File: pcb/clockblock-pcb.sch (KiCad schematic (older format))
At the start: 62 parts

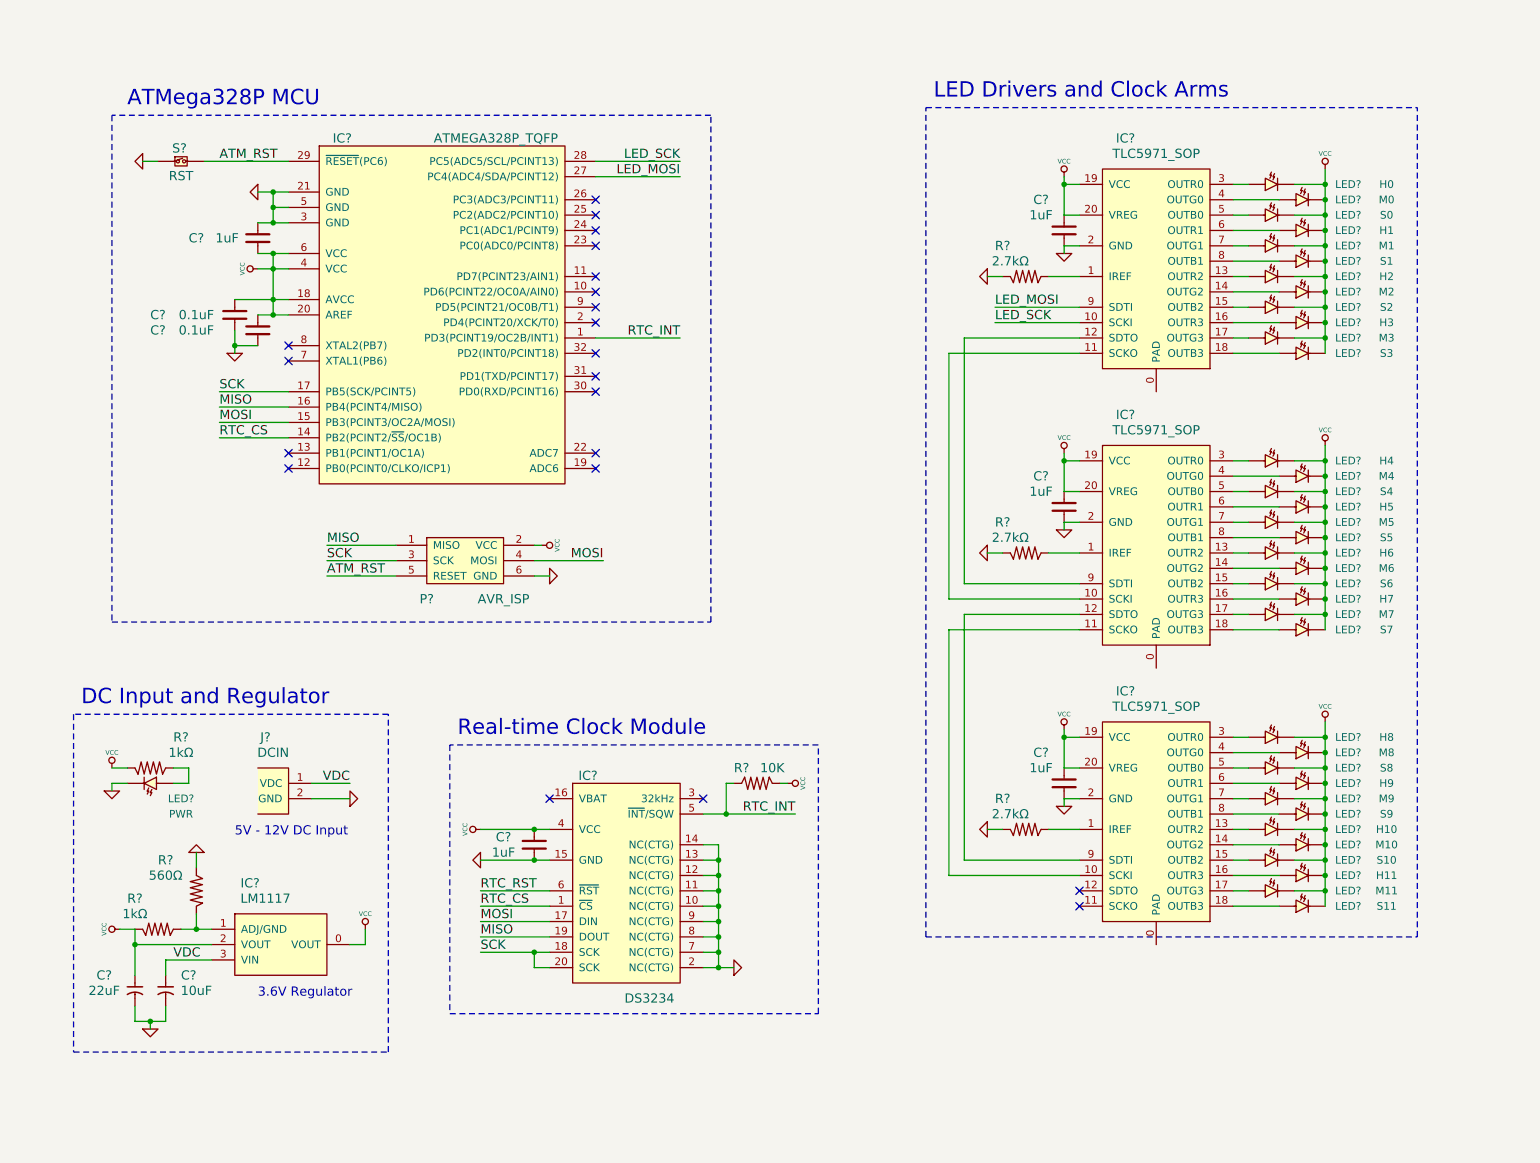
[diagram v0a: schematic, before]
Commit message: fixed incorrect LED polarity, added arm headers, and added a backup coincell for the RTC
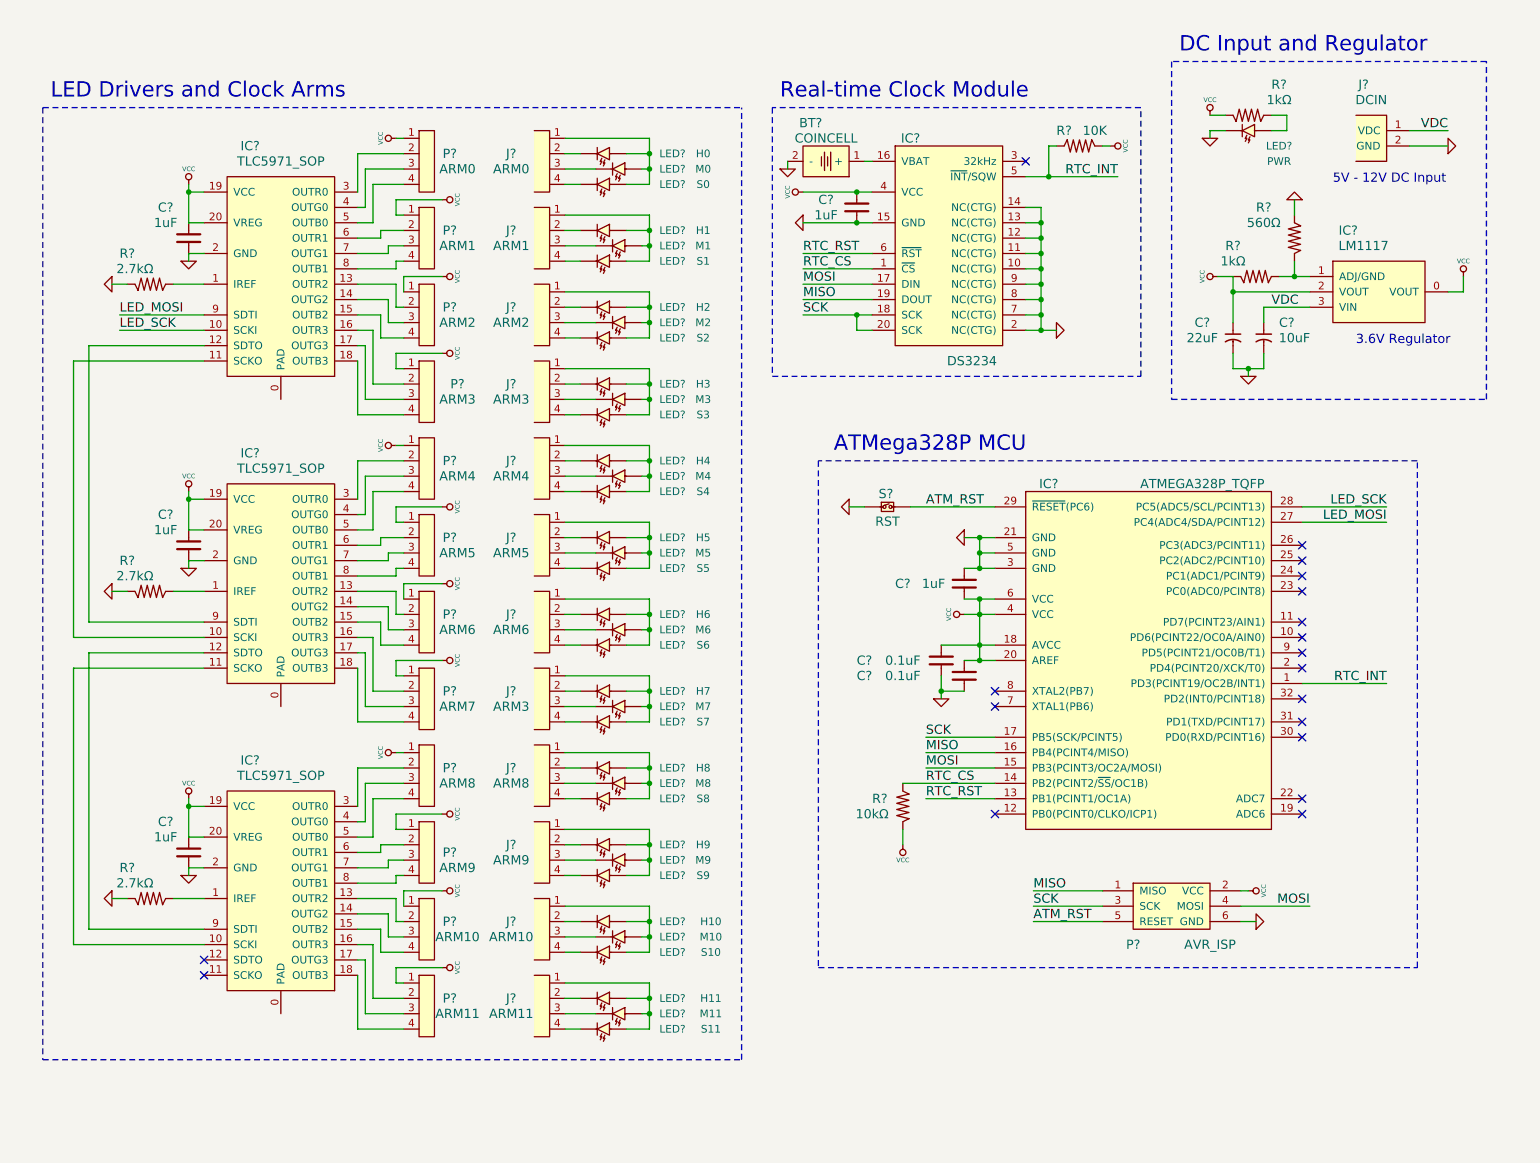
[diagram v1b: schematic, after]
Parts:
- removed LED?: H8, ~, symbol LED
- removed LED?: M8, ~, symbol LED
- removed LED?: S8, ~, symbol LED
- removed LED?: H9, ~, symbol LED
- removed LED?: M9, ~, symbol LED
- removed LED?: S9, ~, symbol LED
- removed LED?: H10, ~, symbol LED
- removed LED?: M10, ~, symbol LED
- removed LED?: S10, ~, symbol LED
- removed LED?: H11, ~, symbol LED
- removed LED?: M11, ~, symbol LED
- removed LED?: S11, ~, symbol LED
- removed LED?: H4, ~, symbol LED
- removed LED?: M4, ~, symbol LED
- removed LED?: S4, ~, symbol LED
- removed LED?: H5, ~, symbol LED
- removed LED?: M5, ~, symbol LED
- removed LED?: S5, ~, symbol LED
- removed LED?: H6, ~, symbol LED
- removed LED?: M6, ~, symbol LED
- removed LED?: S6, ~, symbol LED
- removed LED?: H7, ~, symbol LED
- removed LED?: M7, ~, symbol LED
- removed LED?: S7, ~, symbol LED
- removed LED?: H1, ~, symbol LED
- removed LED?: M1, ~, symbol LED
- removed LED?: S1, ~, symbol LED
- removed LED?: H2, ~, symbol LED
- removed LED?: M2, ~, symbol LED
- removed LED?: S2, ~, symbol LED
- removed LED?: H3, ~, symbol LED
- removed LED?: M3, ~, symbol LED
- removed LED?: S3, ~, symbol LED
- added BT?: COINCELL, symbol BATTERY
- added J?: ARM0, ~, symbol 4PIN_FEMALE
- added J?: ARM1, ~, symbol 4PIN_FEMALE
- added J?: ARM2, ~, symbol 4PIN_FEMALE
- added J? (x2): ARM3, ~, symbol 4PIN_FEMALE
- added J?: ARM4, ~, symbol 4PIN_FEMALE
- added J?: ARM5, ~, symbol 4PIN_FEMALE
- added J?: ARM6, ~, symbol 4PIN_FEMALE
- added J?: ARM8, ~, symbol 4PIN_FEMALE
- added J?: ARM9, ~, symbol 4PIN_FEMALE
- added J?: ARM10, ~, symbol 4PIN_FEMALE
- added J?: ARM11, ~, symbol 4PIN_FEMALE
- added LED?: H1, ~, symbol LED
- added LED?: M1, ~, symbol LED
- added LED?: S1, ~, symbol LED
- added LED?: H2, ~, symbol LED
- added LED?: M2, ~, symbol LED
- added LED?: S2, ~, symbol LED
- added LED?: H3, ~, symbol LED
- added LED?: M3, ~, symbol LED
- added LED?: S3, ~, symbol LED
- added LED?: H4, ~, symbol LED
- added LED?: M4, ~, symbol LED
- added LED?: S4, ~, symbol LED
- added LED?: H5, ~, symbol LED
- added LED?: M5, ~, symbol LED
- added LED?: S5, ~, symbol LED
- added LED?: H6, ~, symbol LED
- added LED?: M6, ~, symbol LED
- added LED?: S6, ~, symbol LED
- added LED?: H7, ~, symbol LED
- added LED?: M7, ~, symbol LED
- added LED?: S7, ~, symbol LED
- added LED?: H8, ~, symbol LED
- added LED?: M8, ~, symbol LED
- added LED?: S8, ~, symbol LED
- added LED?: H9, ~, symbol LED
- added LED?: M9, ~, symbol LED
- added LED?: S9, ~, symbol LED
- added LED?: H10, ~, symbol LED
- added LED?: M10, ~, symbol LED
- added LED?: S10, ~, symbol LED
- added LED?: H11, ~, symbol LED
- added LED?: M11, ~, symbol LED
- added LED?: S11, ~, symbol LED
- added P?: ARM0, ~, symbol 4PIN_HEADER
- added P?: ARM1, ~, symbol 4PIN_HEADER
- added P?: ARM2, ~, symbol 4PIN_HEADER
- added P?: ARM3, ~, symbol 4PIN_HEADER
- added P?: ARM4, ~, symbol 4PIN_HEADER
- added P?: ARM5, ~, symbol 4PIN_HEADER
- added P?: ARM6, ~, symbol 4PIN_HEADER
- added P?: ARM7, ~, symbol 4PIN_HEADER
- added P?: ARM8, ~, symbol 4PIN_HEADER
- added P?: ARM9, ~, symbol 4PIN_HEADER
- added P?: ARM10, ~, symbol 4PIN_HEADER
- added P?: ARM11, ~, symbol 4PIN_HEADER
- added R?: 10kΩ, ~, symbol R
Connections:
- net GND: now also BT?.2 (-)
- net RTC_CS: now also R?.2
- net RTC_RST: now also IC?.13 (PB1(PCINT1/OC1A))
- net VCC: now also P?.1, P?.1, P?.1, P?.1, P?.1, P?.1, P?.1, P?.1, P?.1, P?.1, P?.1, P?.1, R?.1; no longer LED?.1 (C), LED?.1 (C), LED?.1 (C)
- net at IC?.16 (VBAT): now also BT?.1 (+)
- net at IC?.13 (OUTR2): now also P?.2 (x3)
- net at IC?.14 (OUTG2): now also P?.3 (x3)
- net at IC?.15 (OUTB2): now also P?.4 (x3)
- net at IC?.16 (OUTR3): now also P?.2 (x3)
- net at IC?.17 (OUTG3): now also P?.3 (x3)
- net at IC?.18 (OUTB3): now also P?.4 (x3)
- net at IC?.3 (OUTR0): now also P?.2 (x2)
- net at IC?.4 (OUTG0): now also P?.3 (x2)
- net at IC?.5 (OUTB0): now also P?.4 (x2)
- net at IC?.6 (OUTR1): now also P?.2 (x3)
- net at IC?.7 (OUTG1): now also P?.3 (x3)
- net at IC?.8 (OUTB1): now also P?.4 (x3)
- net at IC?.3 (OUTR0): now also P?.2; no longer LED?.2 (A)
- net at IC?.4 (OUTG0): now also P?.3; no longer LED?.2 (A)
- net at IC?.5 (OUTB0): now also P?.4; no longer LED?.2 (A)
- new net: J?.2, LED?.1 (C) (x12)
- new net: J?.1, LED?.2 (A), LED?.2 (A), LED?.2 (A) (x12)
- new net: J?.3, LED?.1 (C) (x12)
- new net: J?.4, LED?.1 (C) (x12)
- no-connect marks 21 -> 19
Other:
- moved on the sheet: C?, IC?, J?, LED?, P?, R?, S?

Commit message: annotated schematic and fixed up a component pin type error
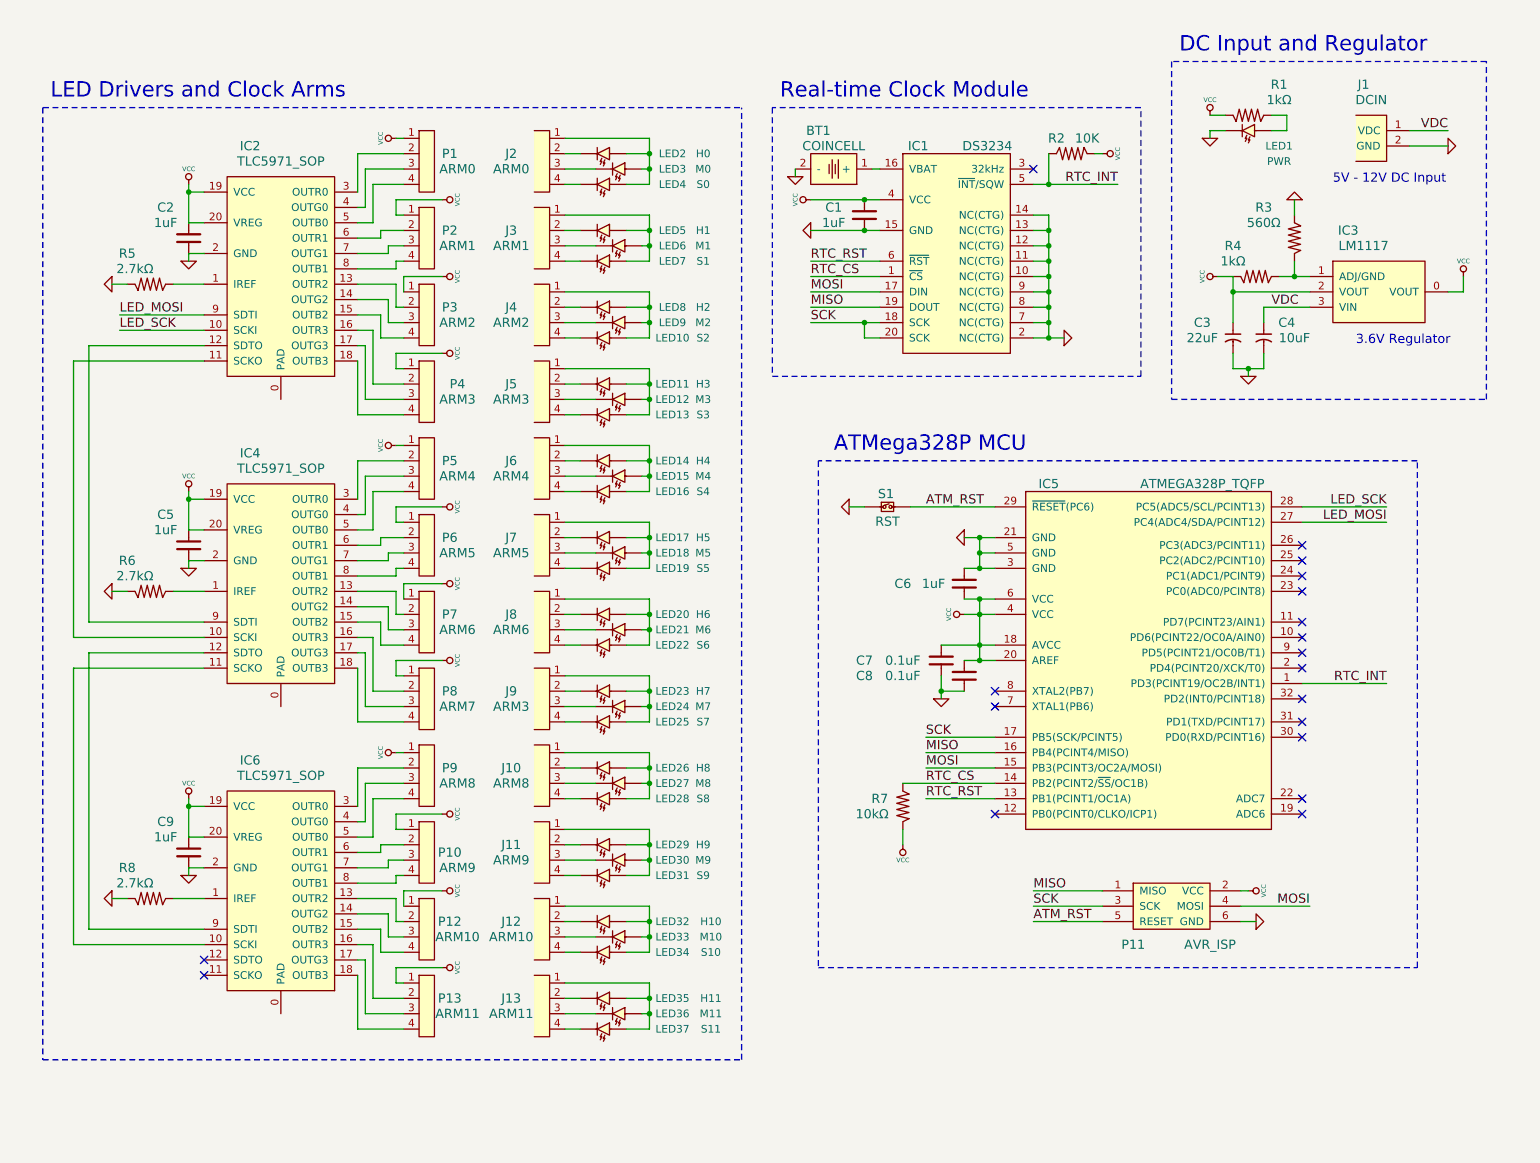
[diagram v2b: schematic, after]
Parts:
- gave numbers to parts that had none: 88
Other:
- moved on the sheet: BT1, C1, IC1, R2

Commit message: component footprints done, moving onto layout
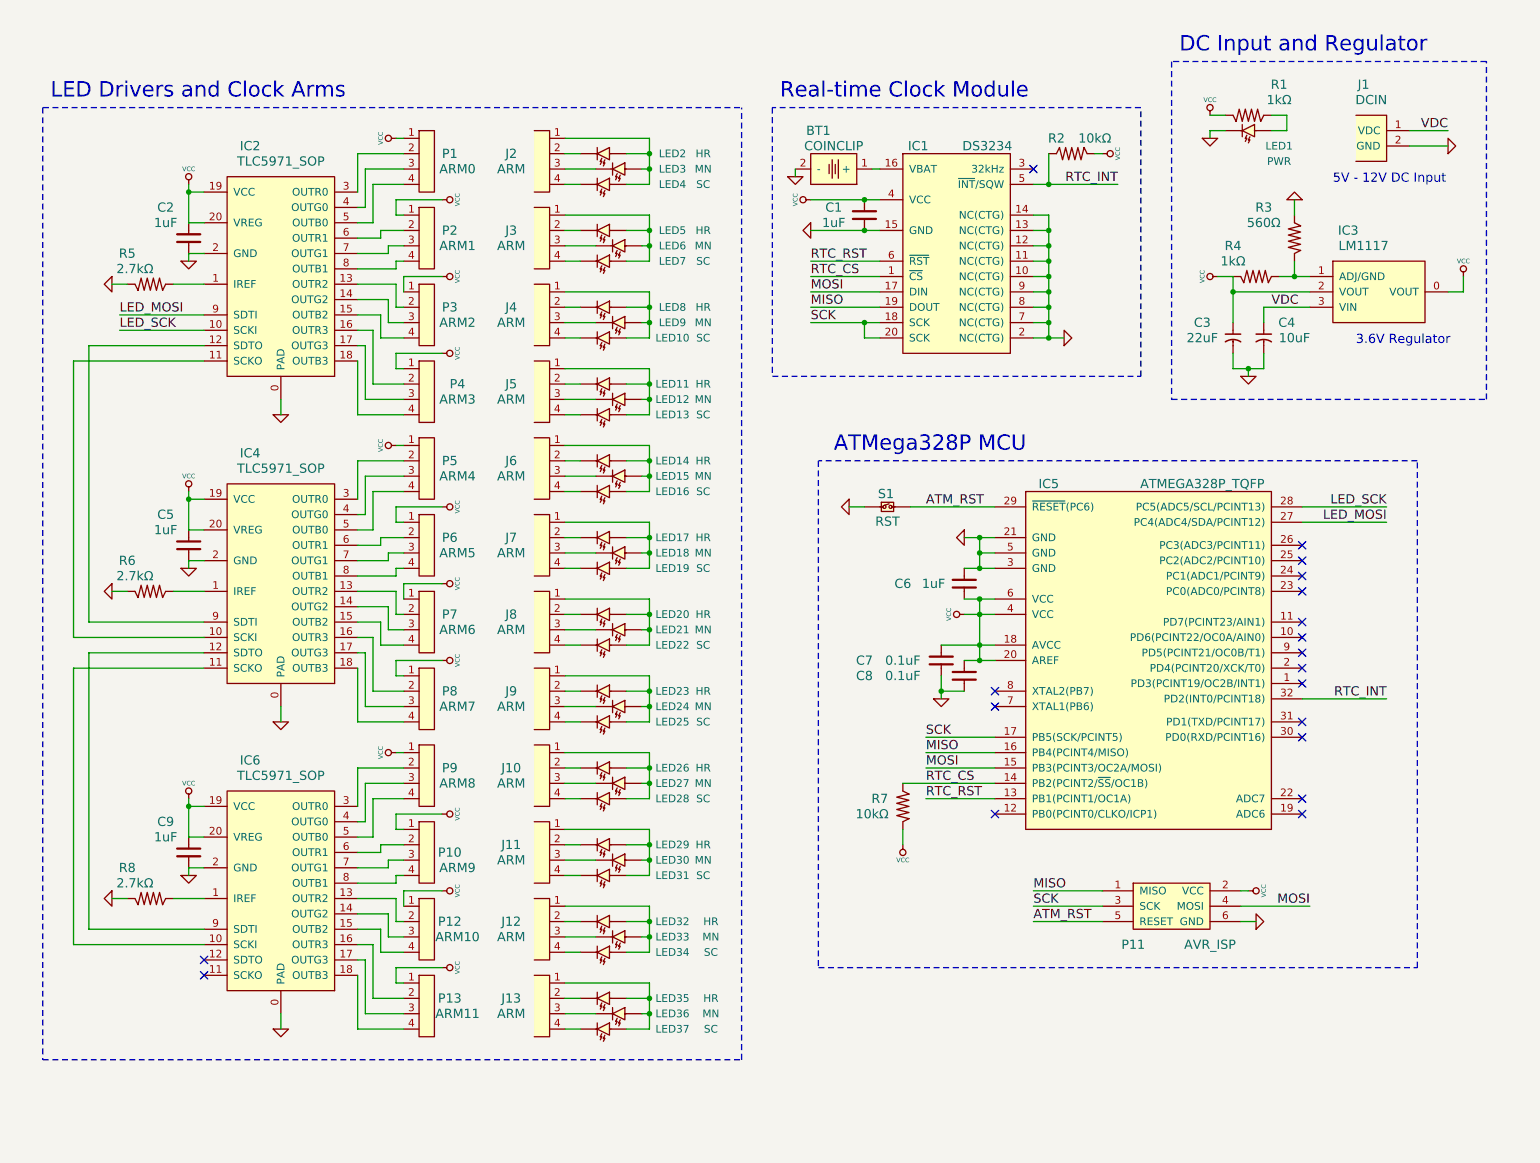
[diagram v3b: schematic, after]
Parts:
- BT1: value COINCELL -> COINCLIP
- J10: value ARM8 -> ARM
- J11: value ARM9 -> ARM
- J12: value ARM10 -> ARM
- J13: value ARM11 -> ARM
- J2: value ARM0 -> ARM
- J3: value ARM1 -> ARM
- J4: value ARM2 -> ARM
- J5, J9: value ARM3 -> ARM
- J6: value ARM4 -> ARM
- J7: value ARM5 -> ARM
- J8: value ARM6 -> ARM
- LED10: value S2 -> SC
- LED11: value H3 -> HR
- LED12: value M3 -> MN
- LED13: value S3 -> SC
- LED14: value H4 -> HR
- LED15: value M4 -> MN
- LED16: value S4 -> SC
- LED17: value H5 -> HR
- LED18: value M5 -> MN
- LED19: value S5 -> SC
- LED2: value H0 -> HR
- LED20: value H6 -> HR
- LED21: value M6 -> MN
- LED22: value S6 -> SC
- LED23: value H7 -> HR
- LED24: value M7 -> MN
- LED25: value S7 -> SC
- LED26: value H8 -> HR
- LED27: value M8 -> MN
- LED28: value S8 -> SC
- LED29: value H9 -> HR
- LED3: value M0 -> MN
- LED30: value M9 -> MN
- LED31: value S9 -> SC
- LED32: value H10 -> HR
- LED33: value M10 -> MN
- LED34: value S10 -> SC
- LED35: value H11 -> HR
- LED36: value M11 -> MN
- LED37: value S11 -> SC
- LED4: value S0 -> SC
- LED5: value H1 -> HR
- LED6: value M1 -> MN
- LED7: value S1 -> SC
- LED8: value H2 -> HR
- LED9: value M2 -> MN
- R2: value 10K -> 10kΩ
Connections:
- net GND: now also IC2.0 (PAD), IC4.0 (PAD), IC6.0 (PAD)
- net RTC_INT: now also IC5.32 (PD2(INT0/PCINT18)); no longer IC5.1 (PD3(PCINT19/OC2B/INT1))

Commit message: board layout done. double checking then sending to fab
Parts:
- added P14: SERIAL, ~, symbol 4PIN_HEADER
- added R10, R9: 10kΩ, ~, symbol R
- added S2, S3: SET, ~, symbol SPST
- C7: value 0.1uF -> 1uF
- IC2, IC4, IC6: value TLC5971_SOP -> TLC5971
- IC5: value ATMEGA328P_TQFP -> ATMEGA328P
- R3: value 560Ω -> 1kΩ
- R4: value 1kΩ -> 560Ω
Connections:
- net GND: now also C7.2, C8.2, P14.4, S2.2, S3.2; no longer C7.1, C8.1
- net RTC_CS: now also IC5.25 (PC2(ADC2/PCINT10)); no longer IC5.14 (PB2(PCINT2/~SS~/OC1B))
- net RTC_RST: now also IC5.26 (PC3(ADC3/PCINT11)); no longer IC5.13 (PB1(PCINT1/OC1A))
- net VCC: now also C7.1, C8.1, P14.3, R10.2, R9.2; no longer C7.2, C8.2
- net at IC5.10 (PD6(PCINT22/OC0A/AIN0)): now also R10.1, S3.1
- net at IC5.11 (PD7(PCINT23/AIN1)): now also R9.1, S2.1
- net at IC5.30 (PD0(RXD/PCINT16)): now also P14.2
- net at IC5.31 (PD1(TXD/PCINT17)): now also P14.1
- no-connect marks 19 -> 15
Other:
- note added: "3.5V Regulator"
- note removed: "3.6V Regulator"
- moved on the sheet: C6, C7, C8, R7

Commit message: moving on to v0.2 schematic
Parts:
- removed BT1: COINCLIP, symbol BATTERY
- removed C1: 1uF, ~, symbol C
- removed IC1: DS3234, symbol DS3234
- removed J1: DCIN, symbol DCIN
- removed J10, J11, J12, J13, J2, J3, J4, J5, J6, J7, J8, J9: ARM, ~, symbol 4PIN_FEMALE
- removed LED10, LED13, LED16, LED19, LED22, LED25, LED28, LED31, LED34, LED37, LED4, LED7: SC, ~, symbol LED
- removed LED11, LED14, LED17, LED2, LED20, LED23, LED26, LED29, LED32, LED35, LED5, LED8: HR, ~, symbol LED
- removed LED12, LED15, LED18, LED21, LED24, LED27, LED3, LED30, LED33, LED36, LED6, LED9: MN, ~, symbol LED
- removed P14: SERIAL, ~, symbol 4PIN_HEADER
- removed R2, R7: 10kΩ, ~, symbol R
- removed R3: 1kΩ, ~, symbol R
- removed R4: 560Ω, ~, symbol R
- R10, R9: value 10kΩ -> opt10kΩ
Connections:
- net labels removed: RTC_CS, RTC_INT, RTC_RST, VDC
- wire segments 361 -> 213
- no-connect marks 15 -> 14
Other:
- note added: "USB Input and Regulator"
- note removed: "5V - 12V DC Input"
- note removed: "DC Input and Regulator"
- note removed: "Real-time Clock Module"
